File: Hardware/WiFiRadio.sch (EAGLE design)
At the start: 55 parts, among them IC1 VS1053B, IC2 23LCV1024-I/SN, IC3 MCP1703AT-1802E/CB, IC4 MCP1703AT-3302E/CB, J1 ADC, J2 RAM, K1 STX-3100-5N, K2 SERIAL, K3 PANEL, K4 POWER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

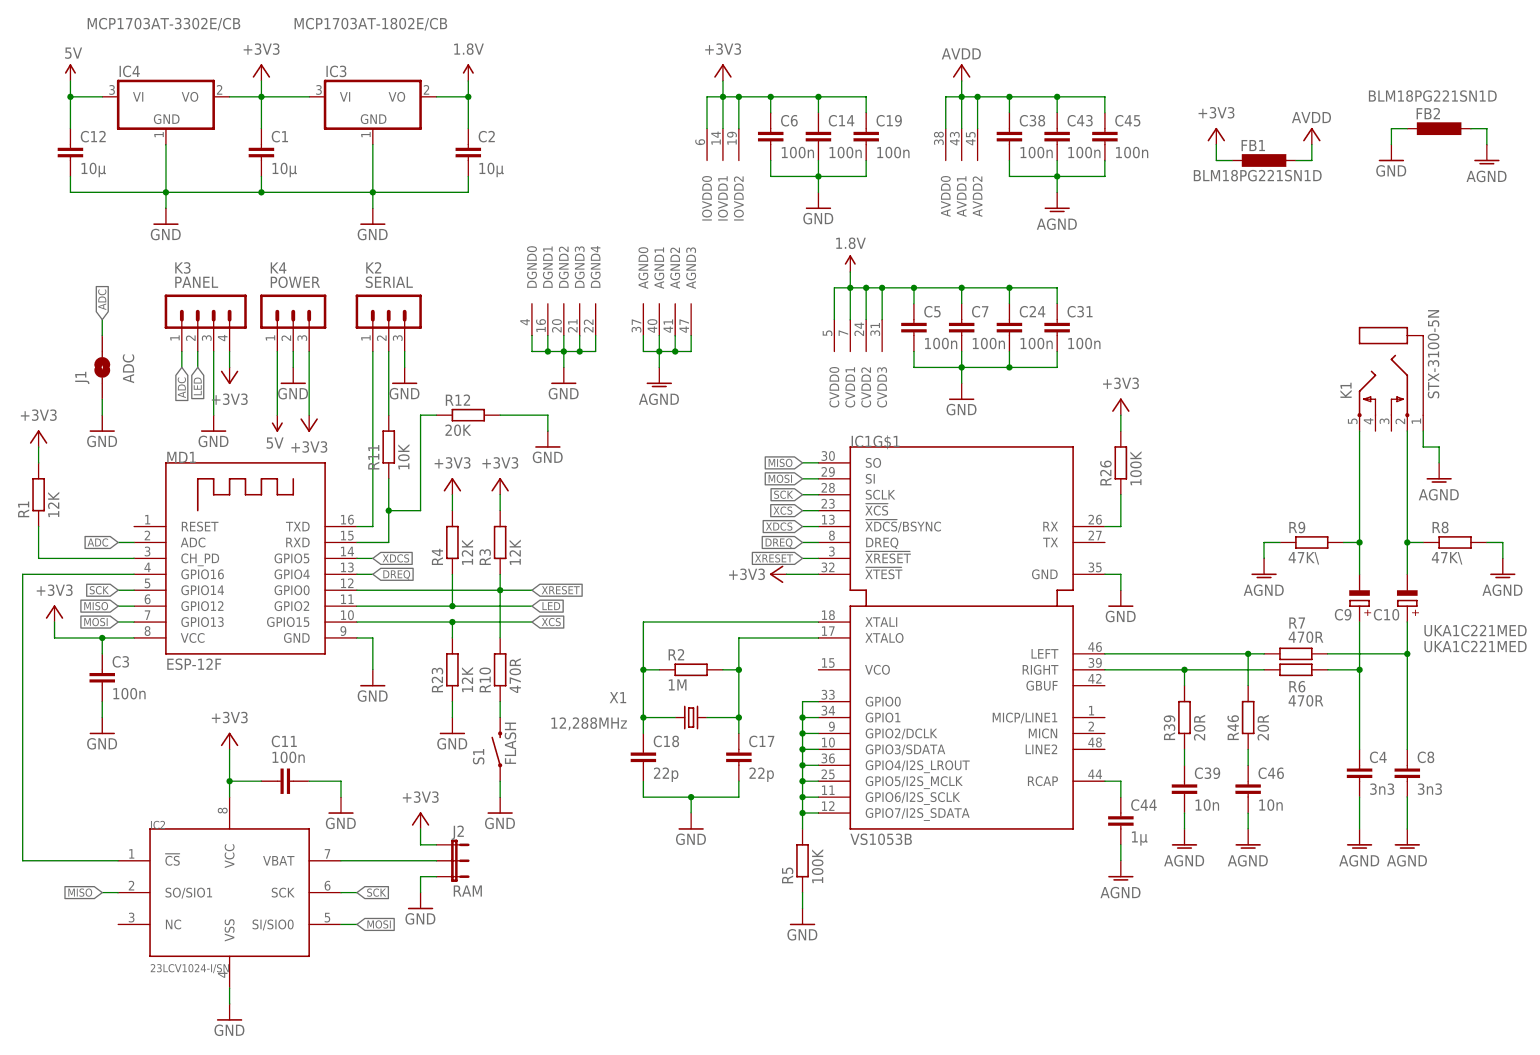
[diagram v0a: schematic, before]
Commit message: new (smaller) pcb for personal needs, removed 5v and 3v3 regulators, added other small improvements
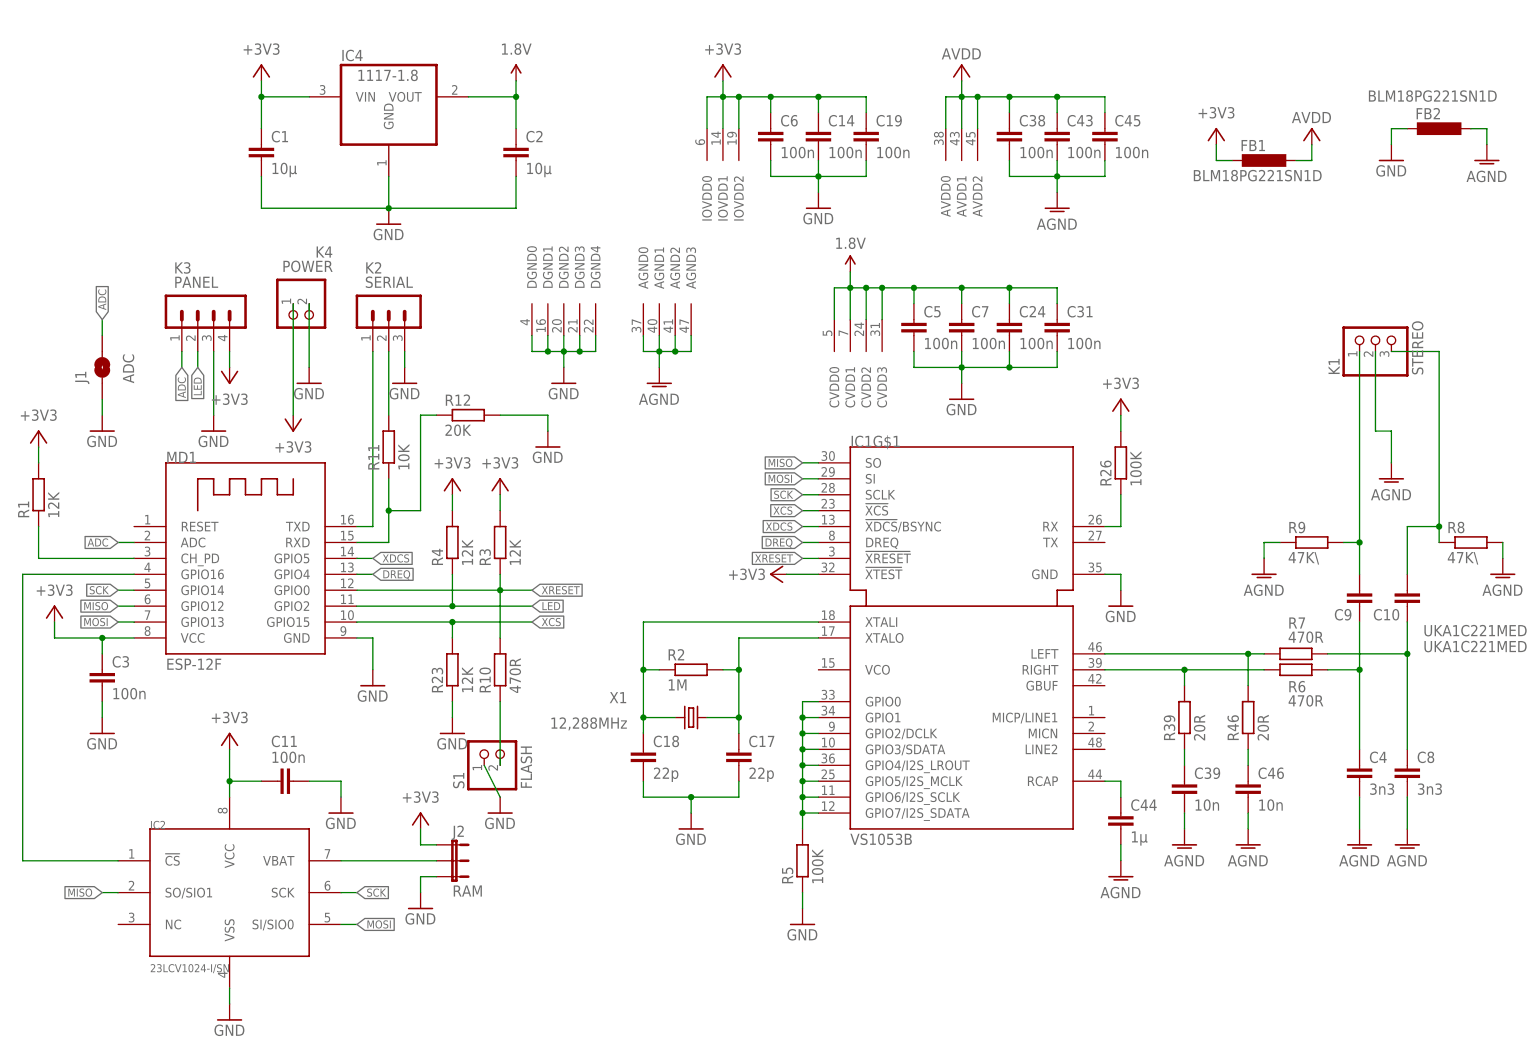
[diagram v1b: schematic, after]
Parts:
- removed C12: 10μ, rcl:C-EUC0805
- removed IC3: MCP1703AT-1802E/CB, linear:MCP1703CB
- C10, C9: device rcl:CPOL-EUE2.5-7 -> rcl:C-EUC0805
- IC4: value MCP1703AT-3302E/CB -> 1117-1.8; device linear:MCP1703CB -> burr-brown:REG1117
- K1: value STX-3100-5N -> STEREO; device adafruit:STEREOJACK -> pinhead:PINHD-1X3
- K4: device con-lstb:MA03-1 -> pinhead:PINHD-1X2
- S1: device SparkFun-Electromechanical:SWITCH-MOMENTARY-2SMD -> pinhead:PINHD-1X2
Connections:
- removed net 5V: C12.1, IC4.VI, K4.1
- net +3V3: now also IC4.VIN, K4.1; no longer IC3.VI, IC4.VO, K4.3
- net 1.8V: now also IC4.VOUT; no longer IC3.VO
- net AGND: now also K1.2; no longer K1.1
- net GND: no longer C12.2, IC3.GND
- net N$14: now also C9.2, K1.1; no longer C9.-, K1.5
- net N$15: now also C10.2, K1.3; no longer C10.-, K1.2
- net N$7: now also C9.1; no longer C9.+
- net N$8: now also C10.1; no longer C10.+
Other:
- moved on the sheet: C2, IC4, R8
